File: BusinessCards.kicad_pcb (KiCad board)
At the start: 2 copper layers, 88.9 x 50.8 mm, 3 parts

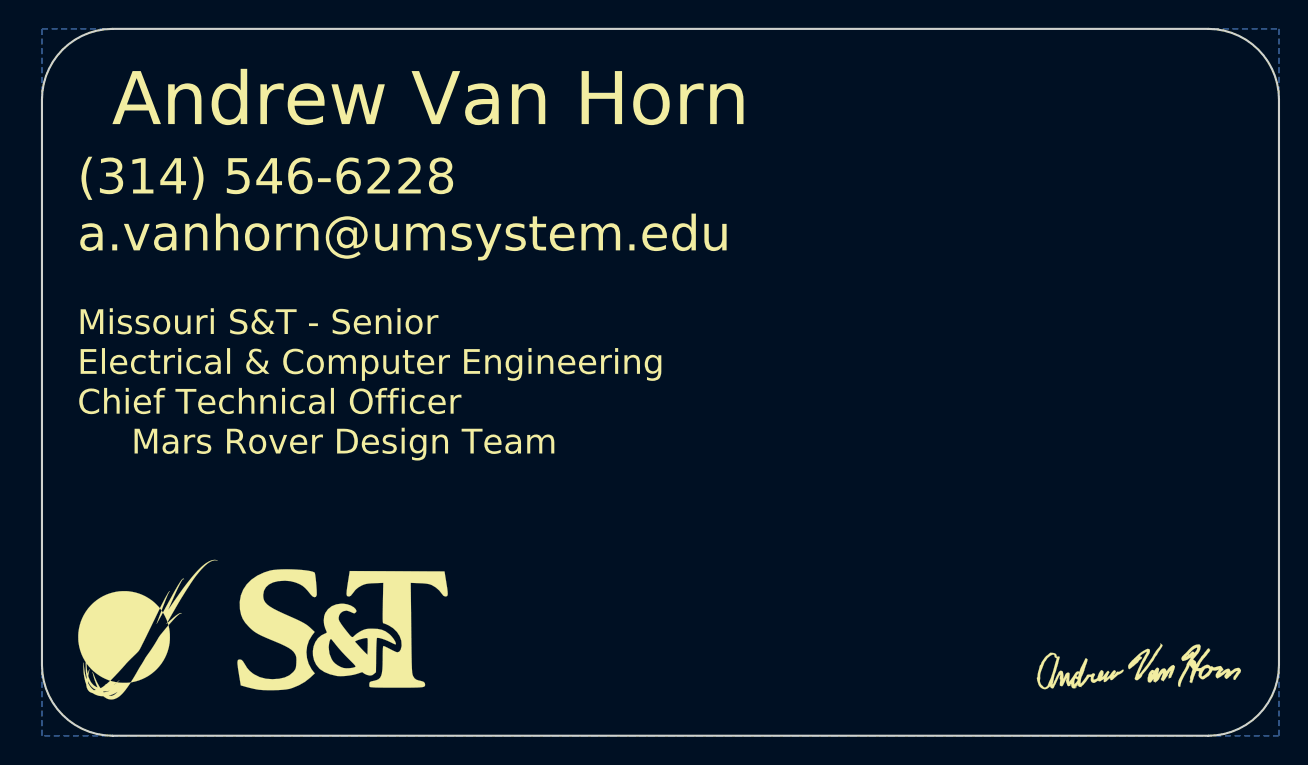
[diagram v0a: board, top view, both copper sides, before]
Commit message: added 5V LDO circuit
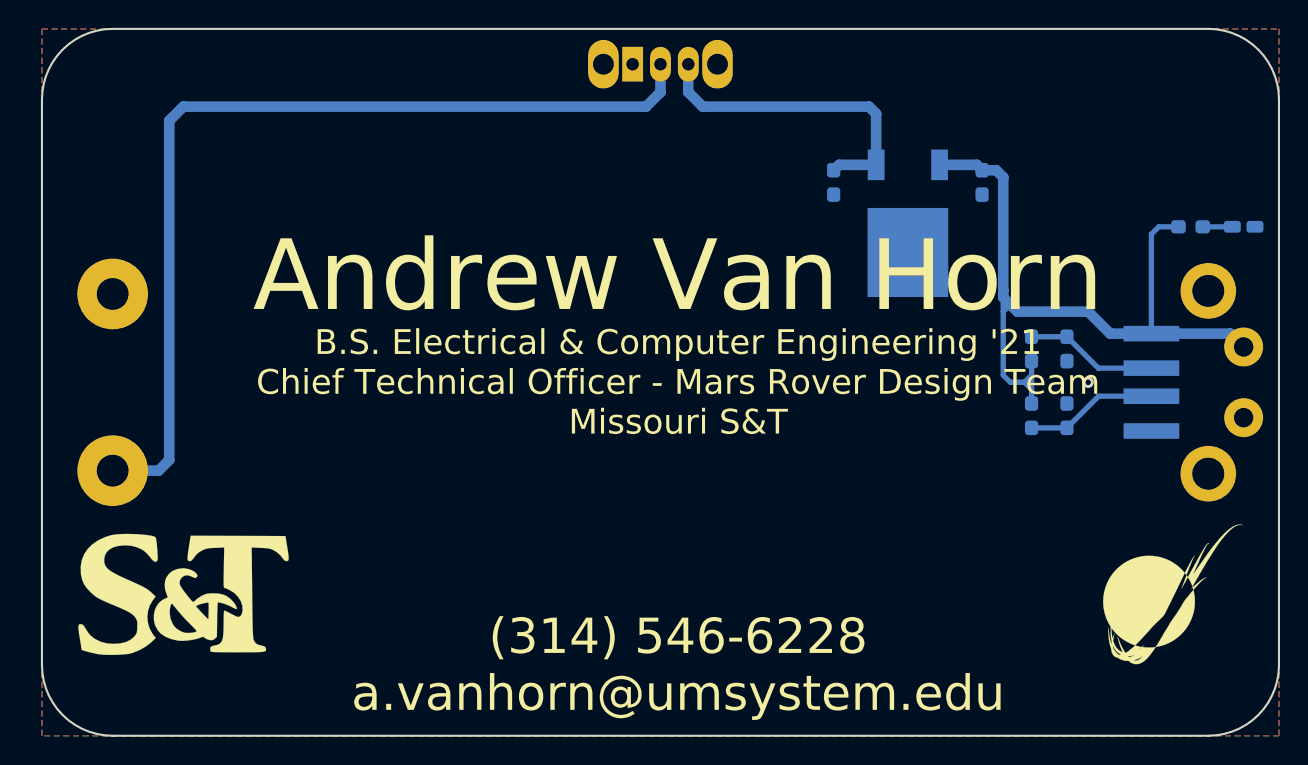
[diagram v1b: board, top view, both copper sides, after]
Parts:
- removed the G*** at (180.3, 96.5)
- added BT1: Battery, ProjectLibrary:9V Battery Holder_36-1294-ND, B.Cu at (106.7, 76.2)
- added C1: 10uF, Capacitor_SMD:C_0603_1608Metric_Pad1.05x0.95mm_HandSolder, B.Cu at (158.5, 61.8)
- added C2: 10uF, Capacitor_SMD:C_0603_1608Metric_Pad1.05x0.95mm_HandSolder, B.Cu at (169.2, 61.8)
- added Conn1: USB_A, ProjectLibrary:USB A Receptacle, B.Cu at (181.8, 76.2)
- added D1: LED, LED_SMD:LED_0603_1608Metric_Castellated, B.Cu at (188.0, 65.0)
- added R1: R, Resistor_SMD:R_0603_1608Metric_Pad1.05x0.95mm_HandSolder, B.Cu at (184.2, 65.0)
- added R2: 75K, Resistor_SMD:R_0603_1608Metric_Pad1.05x0.95mm_HandSolder, B.Cu at (172.7, 78.6)
- added R3: 4.99K, Resistor_SMD:R_0603_1608Metric_Pad1.05x0.95mm_HandSolder, B.Cu at (175.3, 78.6)
- added R4: 75K, Resistor_SMD:R_0603_1608Metric_Pad1.05x0.95mm_HandSolder, B.Cu at (172.7, 73.8)
- added R5: 4.99K, Resistor_SMD:R_0603_1608Metric_Pad1.05x0.95mm_HandSolder, B.Cu at (175.3, 73.8)
- added REF**: TestPoint_Loop_D3.50mm_Drill1.4mm_Beaded, TestPoint:TestPoint_Loop_D3.50mm_Drill1.4mm_Beaded, B.Cu at (188.0, 78.7)
- added REF**: TestPoint_Loop_D3.50mm_Drill1.4mm_Beaded, TestPoint:TestPoint_Loop_D3.50mm_Drill1.4mm_Beaded, B.Cu at (188.0, 73.7)
- added SW1: SW_SPST, Button_Switch_THT:SW_CuK_OS102011MA1QN1_SPDT_Angled, B.Cu at (144.1, 53.3)
- added U1: L7805, Package_TO_SOT_SMD:TO-252-2, B.Cu at (163.8, 64.8)
- moved G*** 73.7 mm to (182.9, 91.4)
- moved G*** 11.7 mm to (111.8, 91.4)
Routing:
- net +9V: track 0.00 -> 66.9 mm
- net +5V: track 0.00 -> 55.2 mm
- net Net-(C1-Pad1): track 0.00 -> 23.0 mm
- net Net-(Conn1-Pad3): track 0.00 -> 9.55 mm
- net Net-(Conn1-Pad2): track 0.00 -> 9.55 mm
- net Net-(D1-Pad2): track 0.00 -> 2.12 mm
- net GND: vias 0 -> 1
- added copper zone on B.Cu, net GND
- added copper zone on F.Cu, net GND
- removed copper zone on B.Cu, net (none)
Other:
- board text added: "+"
- board text added: "-"
- board text added: "5V Out"
- board text added: "9-36V"
- board text added: "B.S. Electrical & Computer Engineering '21 Chief Technical Officer - Mars Rover Design Team Missouri S&T"
- board text added: "GND"
- board text added: "Off"
- board text added: "On"
- board text added: "SW1 - OS102011MA1QN1 BT1 - Keystone 1294 Conn1 - 87583-3010RPALF U1 - L7805CV C1, C2 - 10uF, 0603, 16V R1 - 499, 0603 R3, R5 - 4.99K, 0603 R2, R4 - 75K, 0603 D1 - LED 0603"
- board text added: "www.github.com/andrewvh4 www.linkedin.com/in/andrewvanhorn"
- board text removed: "Missouri S&T - Senior Electrical & Computer Engineering Chief Technical Officer Mars Rover Design Team"
